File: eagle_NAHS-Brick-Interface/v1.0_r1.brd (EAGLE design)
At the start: 31.6 x 14.7 mm, 7 parts, among them IC1 FT232RL, J1 NAHS-BRICK-INTERFACE_I-SIDE

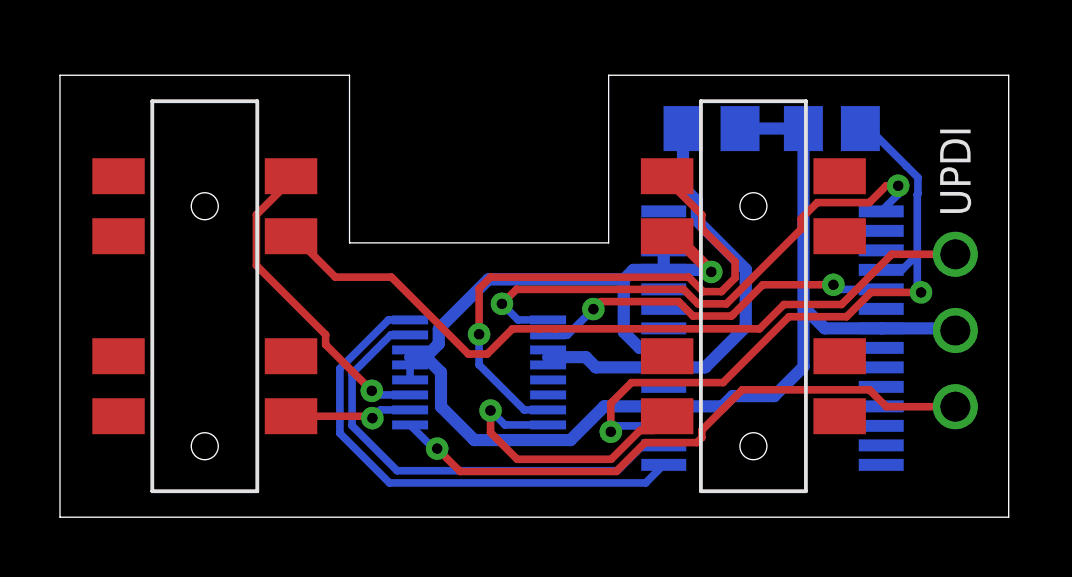
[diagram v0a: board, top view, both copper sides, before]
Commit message: added planes
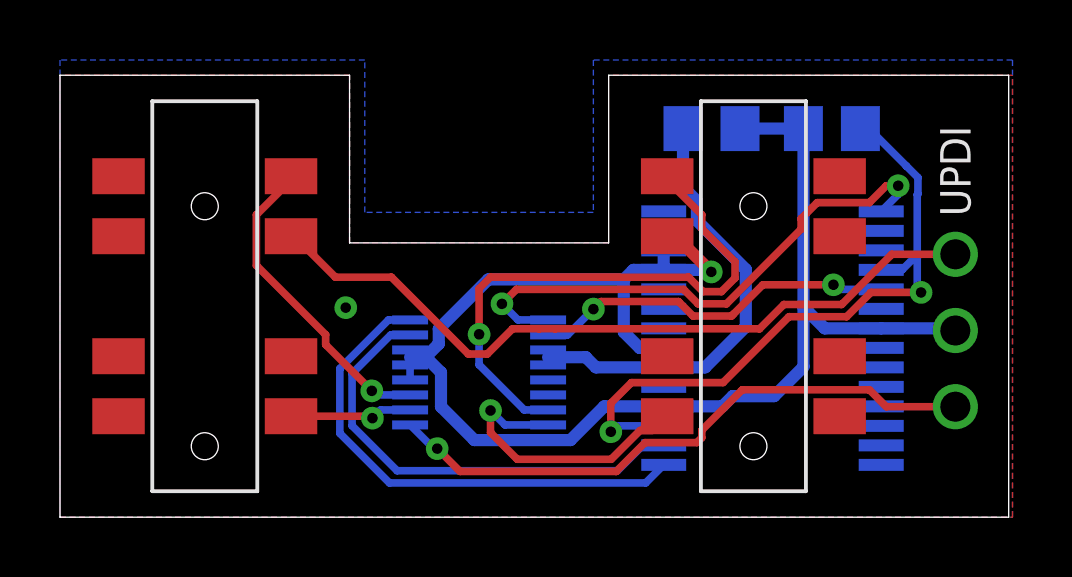
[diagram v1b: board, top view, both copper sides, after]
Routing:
- net GND: vias 1 -> 2
- added copper zone on layer 1, net GND
- added copper zone on layer 16, net GND
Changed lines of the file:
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@@
 <wire x1="24.7832" y1="12.951" x2="24.7802" y2="12.954" width="0.4064" layer="16"/>
 <wire x1="24.7832" y1="7.0032" x2="24.7832" y2="12.951" width="0.4064" layer="16"/>
+<polygon width="0.254" layer="1">
+<vertex x="0" y="0"/>
+<vertex x="31.75" y="0"/>
+<vertex x="31.75" y="14.732"/>
+<vertex x="18.288" y="14.732"/>
+<vertex x="18.288" y="9.144"/>
+<vertex x="9.652" y="9.144"/>
+<vertex x="9.652" y="14.732"/>
+<vertex x="0" y="14.732"/>
+</polygon>
+<polygon width="0.254" layer="16">
+<vertex x="0" y="0"/>
+<vertex x="31.75" y="0"/>
+<vertex x="31.75" y="15.24"/>
+<vertex x="17.78" y="15.24"/>
+<vertex x="17.78" y="10.16"/>
+<vertex x="10.16" y="10.16"/>
+<vertex x="10.16" y="15.24"/>
+<vertex x="0" y="15.24"/>
+</polygon>
+<via x="9.525" y="6.985" extent="1-16" drill="0.35"/>
 </signal>
 <signal name="N$1">
